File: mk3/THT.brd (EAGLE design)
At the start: 31.3 x 44 mm, 13 parts, among them IC1 74HC4053P

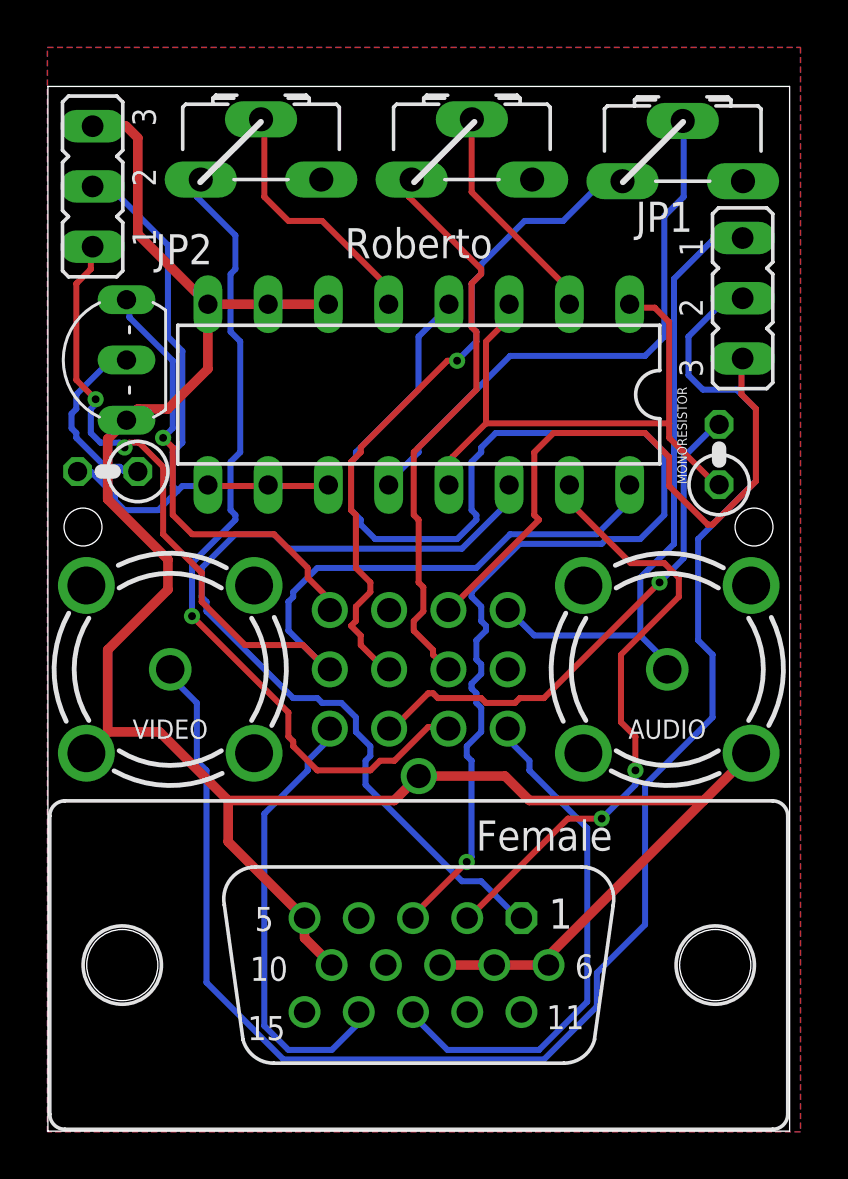
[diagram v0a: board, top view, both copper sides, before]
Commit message: Switched to CD4053, didn't check the ratings on the HC-one.
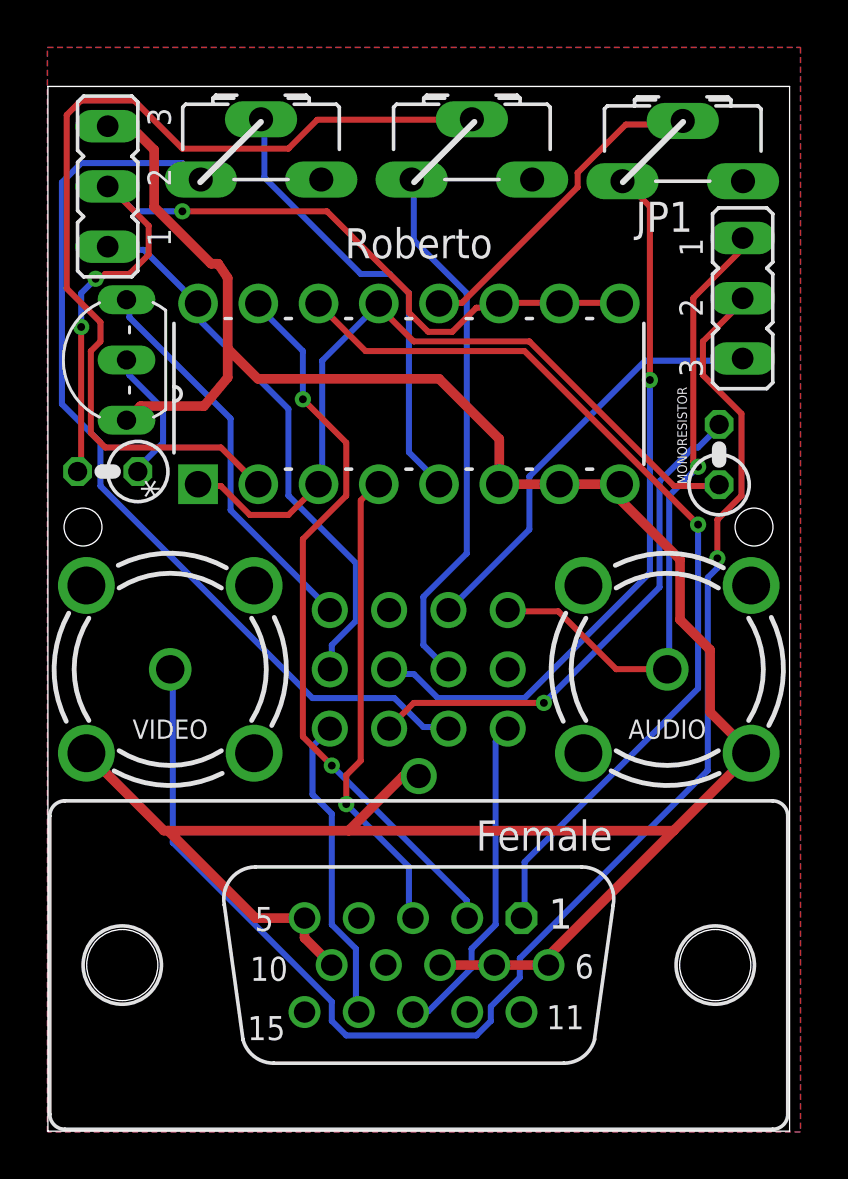
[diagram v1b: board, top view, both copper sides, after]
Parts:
- removed IC1: 74HC4053P, 74xx-eu:DIL16
- added U1: CD4053BCN, Fairchild_By_element14_Batch_1:DIP254P762X508-16
- moved JP2 0.64 mm to (2.54, 39.9)
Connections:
- removed net N$4: IC1.12, R7.S
- removed net N$5: IC1.2, R8.S
- removed net N$6: IC1.5, R9.S
- new net N$1: R8.S, U1.2
- new net N$2: R9.S, U1.5
- new net N$9: R7.S, U1.12
- net GND: now also U1.6, U1.7, U1.8; no longer IC1.6, IC1.7, IC1.8
- net MONOSIGNAL: now also U1.1, U1.13, U1.3; no longer IC1.1, IC1.13, IC1.3
- net SELECT: now also U1.10, U1.11, U1.9; no longer IC1.10, IC1.11, IC1.9
- net VBLUE: now also U1.4; no longer IC1.4
- net VCC: now also U1.16; no longer IC1.16
- net VGREEN: now also U1.15; no longer IC1.15
- net VRED: now also U1.14; no longer IC1.14
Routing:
- net N$1: track 0.00 -> 40.8 mm
- net VBLUE: track 56.3 -> 20.1 mm
- net N$4: track 23.8 -> 0.00 mm
- net VCC: track 45.9 -> 23.5 mm, vias 2 -> 0
- net N$2: track 0.00 -> 19.3 mm
- net GND: track 92.3 -> 108.9 mm
- net N$9: track 0.00 -> 13.8 mm
- net SELECT: track 26.9 -> 39.8 mm, vias 0 -> 3
- net N$6: track 11.0 -> 0.00 mm
- net N$5: track 9.51 -> 0.00 mm
- net AVIDEO: track 26.5 -> 18.1 mm
- net N$3: track 69.2 -> 61.0 mm, vias 0 -> 1
- net AHSYNC: track 21.8 -> 14.0 mm
- net MONOSIGNAL: track 26.3 -> 32.4 mm
- net AVSYNC: track 19.0 -> 13.1 mm
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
